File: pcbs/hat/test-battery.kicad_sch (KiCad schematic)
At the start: 15 parts, among them J2 Conn_01x02_Female, Q1 Q_NMOS_DGS, Q2 Q_NMOS_DGS, U2 INA195, U3 TP5000-Breakout-Akaddy

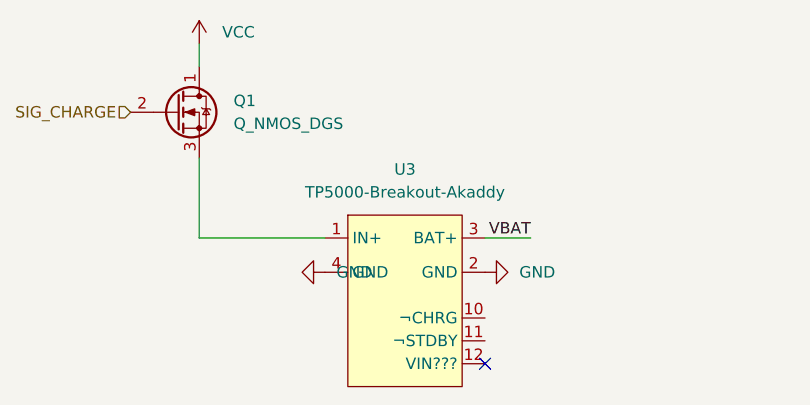
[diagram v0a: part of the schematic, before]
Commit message: fix symbol and footprint libraries
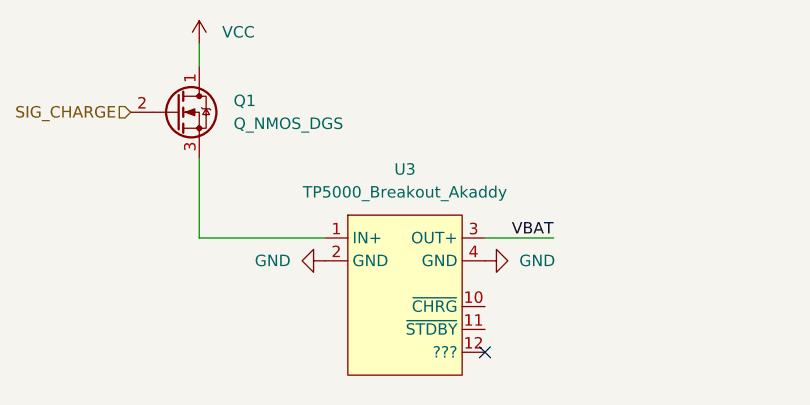
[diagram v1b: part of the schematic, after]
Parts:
- removed U3: TP5000-Breakout-Akaddy, symbol STS_Battery_Management:TP5000-Breakout-Akaddy
- added U3: TP5000_Breakout_Akaddy, symbol STS_Battery_Management:TP5000_Breakout_Akaddy
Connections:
- net GND: now also U3.2 (GND), U3.4 (GND)
- net VBAT: now also U3.3 (OUT+)
- net at Q1.3 (S): now also U3.1 (IN+)
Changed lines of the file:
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@@
   (junction (at 107.95 45.72) (diameter 0) (color 0 0 0 0)
   )
-  (no_connect (at 102.87 147.32))
+  (no_connect (at 102.87 146.05))
   (wire (pts (xy 71.12 133.35) (xy 85.09 133.35))
     (stroke (width 0) (type default) (color 0 0 0 0))
@@
     (stroke (width 0) (type default) (color 0 0 0 0))
   )
-  (wire (pts (xy 107.95 133.35) (xy 102.87 133.35))
+  (wire (pts (xy 102.87 133.35) (xy 110.49 133.35))
     (stroke (width 0) (type default) (color 0 0 0 0))
   )
@@
     (effects (font (size 1.27 1.27)) (justify left bottom))
   )
-  (label "VBAT" (at 107.95 133.35 180)
+  (label "VBAT" (at 110.49 133.35 180)
     (effects (font (size 1.27 1.27)) (justify right bottom))
   )
@@
     (pin "1")
   )
-  (symbol (lib_id "power:GND") (at 102.87 137.16 90) (unit 1)
-    (in_bom yes) (on_board yes) (fields_autoplaced)
-    (property "Reference" "#PWR0105" (id 0) (at 109.22 137.16 0)
-      (effects (font (size 1.27 1.27)) hide)
-    )
-    (property "Value" "GND" (id 1) (at 106.68 137.1599 90)
-      (effects (font (size 1.27 1.27)) (justify right))
-    )
-    (property "Footprint" "" (id 2) (at 102.87 137.16 0)
-      (effects (font (size 1.27 1.27)) hide)
-    )
-    (property "Datasheet" "" (id 3) (at 102.87 137.16 0)
+  (symbol (lib_id "STS_Battery_Management:TP5000_Breakout_Akaddy") (at 87.63 130.81 0) (unit 1)
+    (in_bom yes) (on_board yes) (fields_autoplaced)
+    (property "Reference" "U3" (id 0) (at 93.98 125.73 0))
+    (property "Value" "TP5000_Breakout_Akaddy" (id 1) (at 93.98 128.27 0))
+    (property "Footprint" "" (id 2) (at 87.63 129.54 0)
+      (effects (font (size 1.27 1.27)) hide)
+    )
+    (property "Datasheet" "https://www.amazon.de/Akaddy-TP5000-Lithium-Ionen-LiFePO4-Ladekarten-Lademodul/dp/B07X935CKF" (id 3) (at 87.63 129.54 0)
+      (effects (font (size 1.27 1.27)) hide)
+    )
+    (pin "1")
+    (pin "10")
+    (pin "11")
+    (pin "12")
+    (pin "2")
+    (pin "3")
+    (pin "4")
+  )
+  (symbol (lib_id "power:GND") (at 102.87 135.89 90) (unit 1)
+    (in_bom yes) (on_board yes)
+    (property "Reference" "#PWR0105" (id 0) (at 109.22 135.89 0)
+      (effects (font (size 1.27 1.27)) hide)
+    )
+    (property "Value" "GND" (id 1) (at 106.68 135.8899 90)
+      (effects (font (size 1.27 1.27)) (justify right))
+    )
+    (property "Footprint" "" (id 2) (at 102.87 135.89 0)
+      (effects (font (size 1.27 1.27)) hide)
+    )
+    (property "Datasheet" "" (id 3) (at 102.87 135.89 0)
       (effects (font (size 1.27 1.27)) hide)
     )
@@
     (pin "2")
   )
-  (symbol (lib_id "power:GND") (at 85.09 137.16 270) (unit 1)
-    (in_bom yes) (on_board yes) (fields_autoplaced)
-    (property "Reference" "#PWR0106" (id 0) (at 78.74 137.16 0)
-      (effects (font (size 1.27 1.27)) hide)
-    )
-    (property "Value" "GND" (id 1) (at 86.36 137.1599 90)
-      (effects (font (size 1.27 1.27)) (justify left))
-    )
-    (property "Footprint" "" (id 2) (at 85.09 137.16 0)
-      (effects (font (size 1.27 1.27)) hide)
-    )
-    (property "Datasheet" "" (id 3) (at 85.09 137.16 0)
+  (symbol (lib_id "power:GND") (at 85.09 135.89 270) (unit 1)
+    (in_bom yes) (on_board yes) (fields_autoplaced)
+    (property "Reference" "#PWR0106" (id 0) (at 78.74 135.89 0)
+      (effects (font (size 1.27 1.27)) hide)
+    )
+    (property "Value" "GND" (id 1) (at 81.28 135.8899 90)
+      (effects (font (size 1.27 1.27)) (justify right))
+    )
+    (property "Footprint" "" (id 2) (at 85.09 135.89 0)
+      (effects (font (size 1.27 1.27)) hide)
+    )
+    (property "Datasheet" "" (id 3) (at 85.09 135.89 0)
       (effects (font (size 1.27 1.27)) hide)
     )
@@
     (pin "2")
   )
-  (symbol (lib_id "STS_Battery_Management:TP5000-Breakout-Akaddy") (at 93.98 130.81 0) (unit 1)
-    (in_bom yes) (on_board yes) (fields_autoplaced)
-    (property "Reference" "U3" (id 0) (at 93.98 125.73 0))
-    (property "Value" "TP5000-Breakout-Akaddy" (id 1) (at 93.98 128.27 0))
-    (property "Footprint" "" (id 2) (at 90.17 133.35 0)
-      (effects (font (size 1.27 1.27)) hide)
-    )
-    (property "Datasheet" "" (id 3) (at 90.17 133.35 0)
-      (effects (font (size 1.27 1.27)) hide)
-    )
-    (pin "1")
-    (pin "10")
-    (pin "11")
-    (pin "12")
-    (pin "2")
-    (pin "3")
-    (pin "4")
-  )
   (symbol (lib_id "Device:R") (at 189.23 137.16 0) (unit 1)

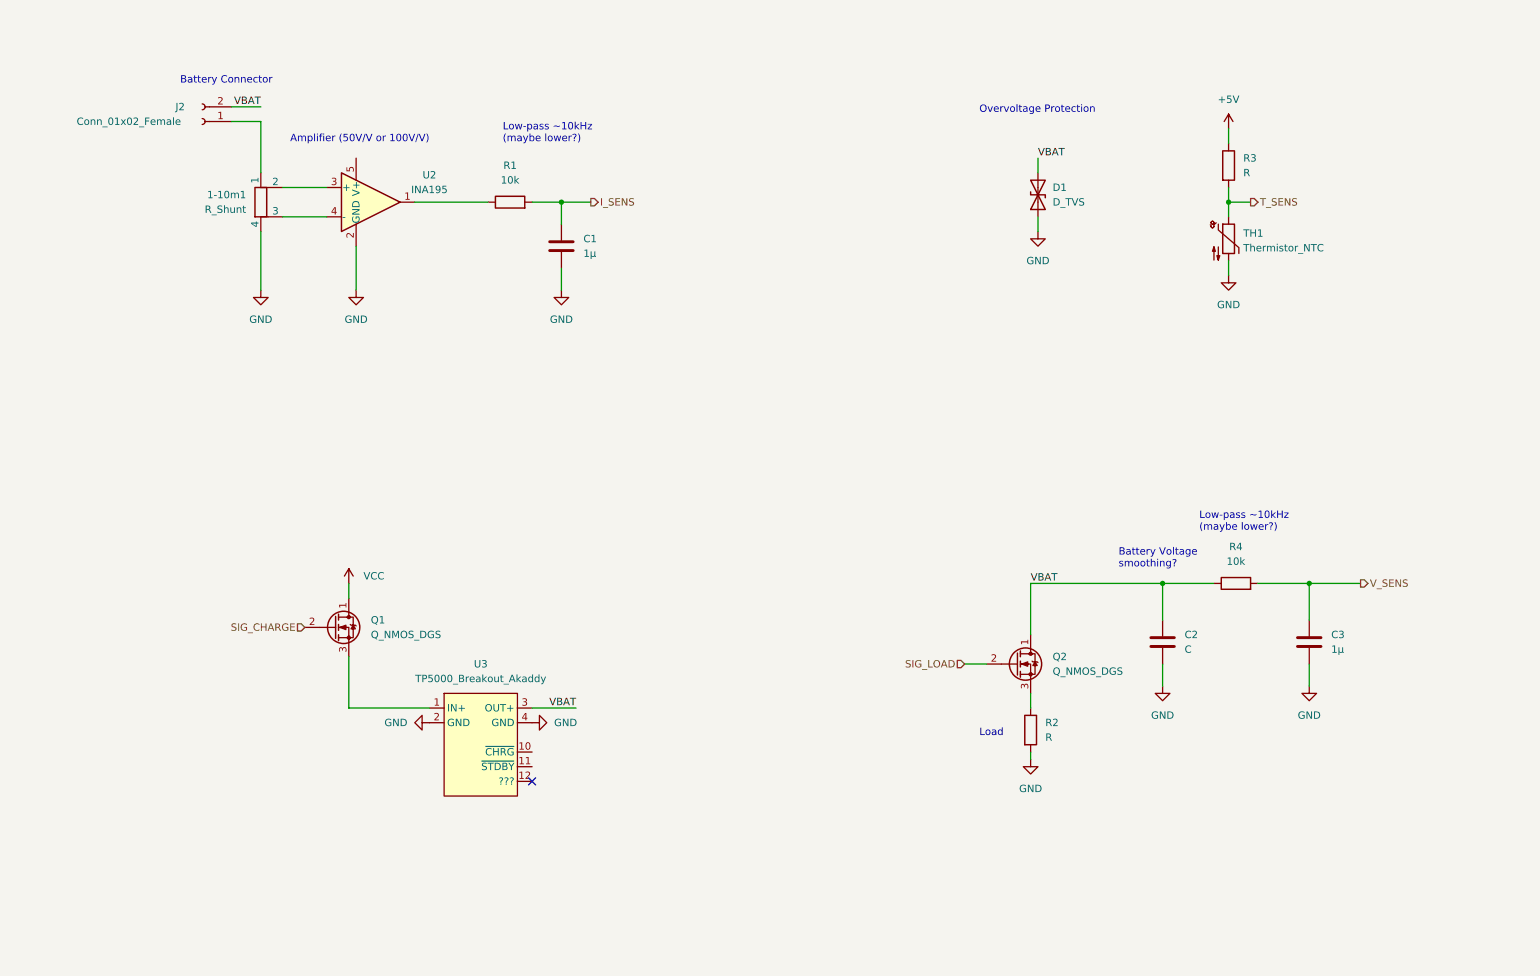
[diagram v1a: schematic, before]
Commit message: add ADCs
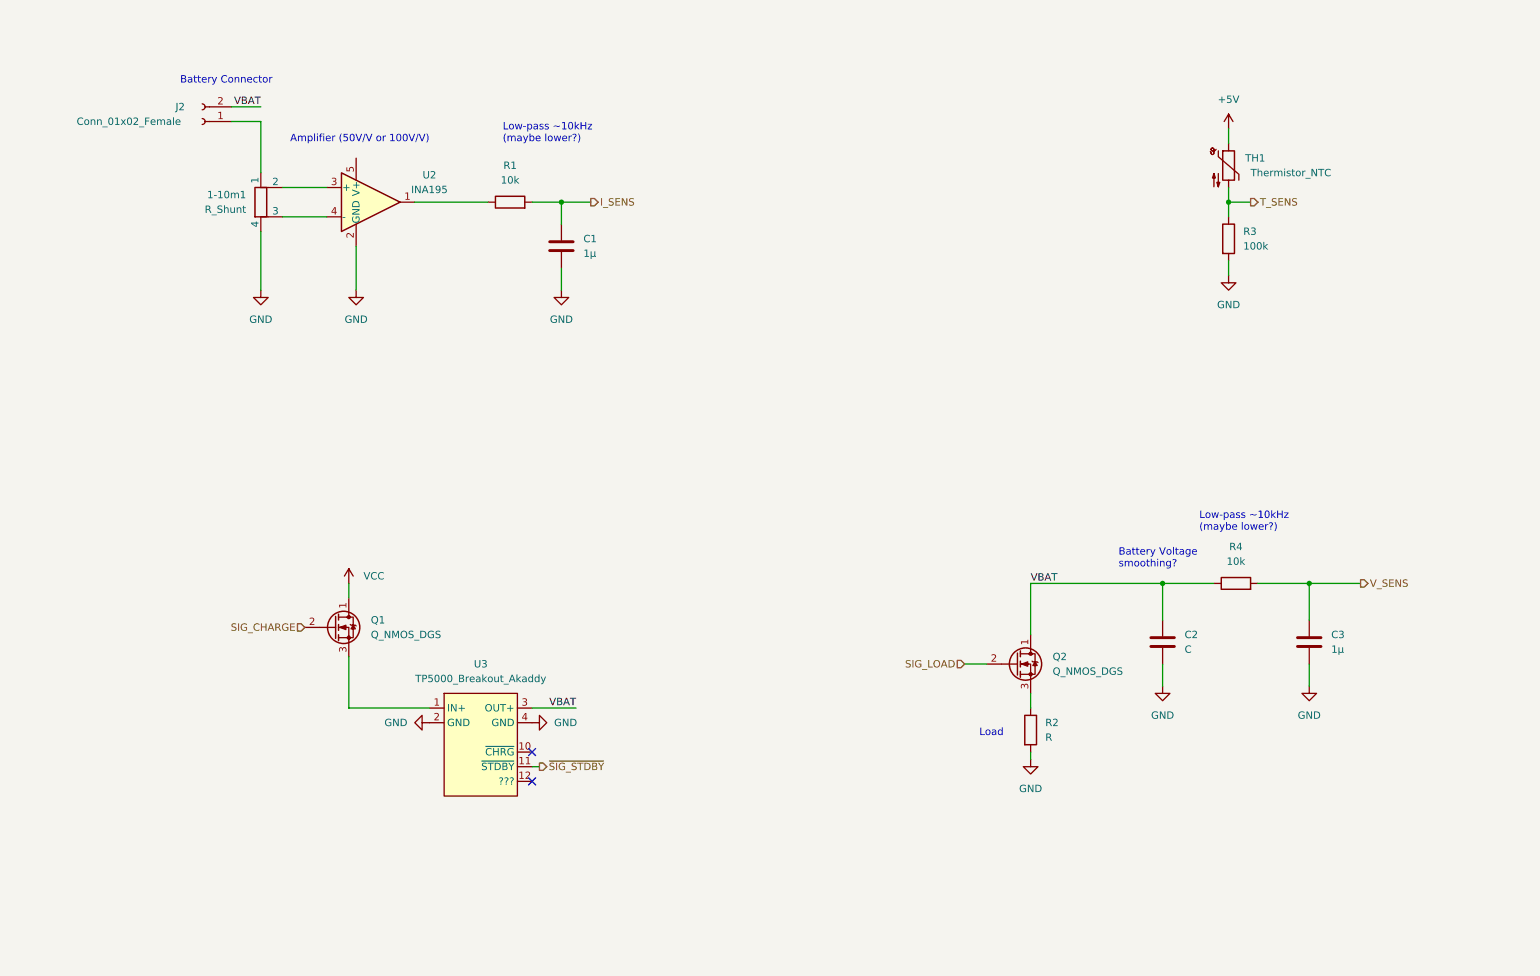
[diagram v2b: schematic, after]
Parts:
- removed D1: D_TVS, symbol Device:D_TVS
- C2: footprint Capacitor_SMD:C_0603_1608Metric -> (none)
- C3: footprint Capacitor_SMD:C_1206_3216Metric -> (none)
- J2: footprint (none) -> TerminalBlock:TerminalBlock_bornier-2_P5.08mm
- Q1, Q2: footprint Package_TO_SOT_THT:TO-251-3-1EP_Horizontal_TabDown -> (none)
- R3: value R -> 100k
- R4: footprint Resistor_SMD:R_0402_1005Metric -> (none)
- TH1: footprint (none) -> Connector_PinHeader_2.54mm:PinHeader_1x02_P2.54mm_Vertical
- U2: footprint Package_TO_SOT_SMD:SOT-23-5 -> (none)
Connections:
- net +5V: now also TH1.1; no longer R3.1
- net GND: now also R3.2; no longer TH1.2
- net T_SENS: now also R3.1, TH1.2; no longer R3.2, TH1.1
- net ~{SIG_STDBY}: now reaches U3.11 (~{STDBY})
- no-connect marks 1 -> 2
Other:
- note removed: "Overvoltage Protection"
- moved on the sheet: R3, TH1

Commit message: select parts for current and temperature sensors
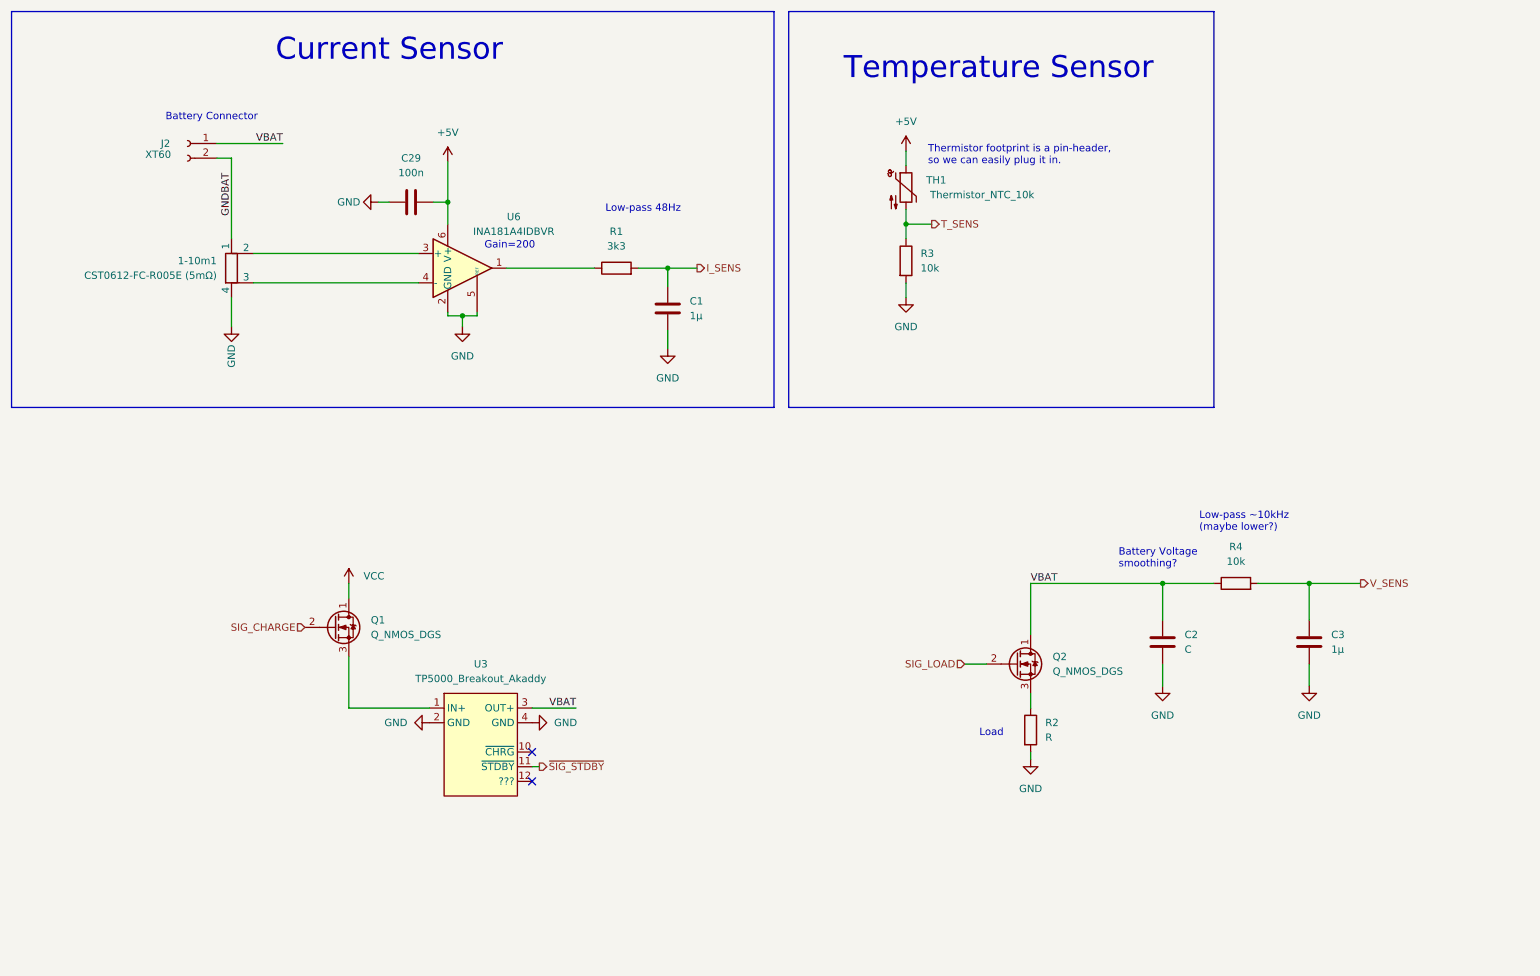
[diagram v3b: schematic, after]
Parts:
- removed U2: INA195, symbol Amplifier_Current:INA195
- added C29: 100n, Capacitor_SMD:C_0603_1608Metric, symbol Device:C
- added U6: INA181A4IDBVR, Package_TO_SOT_SMD:SOT-23-6, symbol Amplifier_Current:INA181
- 1-10m1: value R_Shunt -> CST0612-FC-R005E (5mΩ); footprint (none) -> STS_Resistor_SMD:CST0612-FC-R002E
- C1: footprint (none) -> Capacitor_SMD:C_0603_1608Metric
- J2: value Conn_01x02_Female -> XT60; footprint TerminalBlock:TerminalBlock_bornier-2_P5.08mm -> Connector_AMASS:AMASS_XT60-M_1x02_P7.20mm_Vertical
- R1: value 10k -> 3k3; footprint (none) -> Resistor_SMD:R_0603_1608Metric
- R3: value 100k -> 10k
- TH1: value Thermistor_NTC -> Thermistor_NTC_10k
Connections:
- net +5V: now also C29.2, U6.6 (V+)
- net GND: now also C29.1, U6.2 (GND), U6.5 (REF)
- net VBAT: now also J2.1 (Pin_1); no longer J2.2 (Pin_2)
- net at R1.1: now also U6.1
- net at 1-10m1.2: now also U6.3 (+)
- net at 1-10m1.3: now also U6.4 (-)
- net GNDBAT: now reaches 1-10m1.1
- net GNDBAT: now also J2.2 (Pin_2); no longer J2.1 (Pin_1)
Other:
- note added: "Current Sensor"
- note added: "Gain=200"
- note added: "Low-pass 48Hz"
- note added: "Temperature Sensor"
- note added: "Thermistor footprint is a pin-header, so we can easily plug it in."
- note removed: "Amplifier (50V/V or 100V/V)"
- moved on the sheet: 1-10m1, C1, J2, R1, R3, TH1

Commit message: work on charging circuit
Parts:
- added R35: 680, Resistor_SMD:R_0603_1608Metric, symbol Device:R
- added R36: 10k, Resistor_SMD:R_0603_1608Metric, symbol Device:R
- C3: footprint (none) -> Capacitor_SMD:C_0603_1608Metric
- R3: footprint (none) -> Resistor_SMD:R_0603_1608Metric
- R4: value 10k -> 3k3; footprint (none) -> Resistor_SMD:R_0603_1608Metric
- U3: footprint (none) -> STS_Boards:TP5000_Breakout_Akaddy
- renumbered C29 to C27, U6 to U2
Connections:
- net GND: now also Q1.3 (S), R36.2; no longer U3.2 (GND), U3.4 (GND)
- net SIG_CHARGE: now also R35.1; no longer Q1.2 (G)
- net VCC: now also U3.1 (IN+); no longer Q1.1 (D)
- net ~{SIG_STDBY} renamed ~{SIG_CHRG_DONE}
- new net: Q1.2 (G), R35.2, R36.1
- new net: Q1.1 (D), U3.2 (GND), U3.4 (GND)
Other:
- note added: "Breakout Pictures:"
- note added: "Charging"
- note added: "Datasheet TC5000 (Chip on Breakout)"
- note added: "V_{to} < 3V"
- note added: "max 8mA@3.3V"
- note removed: "Low-pass ~10kHz (maybe lower?)"
- moved on the sheet: Q2, R2, U3

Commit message: more work on charging circuit
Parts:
- removed C3: 1µ, Capacitor_SMD:C_0603_1608Metric, symbol Device:C
- removed Q2: Q_NMOS_DGS, symbol Device:Q_NMOS_DGS
- added #BT1: Battery, symbol Device:Battery_Cell
- added #R1: R_{intern}, symbol Device:R
- added C3: 220u, Capacitor_THT:CP_Radial_D6.3mm_P2.50mm, symbol Device:C_Polarized
- added C5: C, symbol Device:C
- added Q1: Q_NMOS_DGS, Package_TO_SOT_THT:TO-220-3_Vertical, symbol Device:Q_NMOS_DGS
- added R3: 680, Resistor_SMD:R_0603_1608Metric, symbol Device:R
- C2: value C -> 100n; footprint (none) -> Capacitor_SMD:C_0603_1608Metric
- Q2: renamed from Q1; footprint (none) -> Package_TO_SOT_SMD:SOT-223
- R2: value R -> 1; footprint (none) -> Resistor_THT:R_Axial_DIN0617_L17.0mm_D6.0mm_P25.40mm_Horizontal
- R4: value 3k3 -> 10k
- renumbered C27 to C1, C1 to C4, 1-10m1 to R1, R1 to R5, R3 to R6, R35 to R7, R36 to R8, U2 to U1, U3 to U2
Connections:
- net GND: now also R4.2, #BT1.2 (-), C3.2, C5.2, Q1.3 (S); no longer R2.2
- net SIG_LOAD: now also R3.1
- net V_SENS: now also J2.1 (Pin_1), R2.2, U2.3 (OUT+); no longer R4.2
- net at R2.1: now also C3.1, Q1.1 (D)
- net VBAT: no longer names the net of C2.1, R4.1
- net VBAT: now also Q1.2 (G), R3.2; no longer J2.1 (Pin_1), U2.3 (OUT+)
- new net: #BT1.1 (+), #R1.2
- no-connect marks 2 -> 3
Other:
- note added: "Battery"
- note added: "Battery looks like this"
- note added: "Can/Should we put a capacitor here to filter the signal a little?"
- note added: "Datasheet TP5000 (Chip on Breakout)"
- note added: "Discharging"
- note added: "Fake Load"
- note added: "Power Rating > 5W"
- note added: "V_{threshold} < 2V The signal is only 3.3V and the pull down creates a voltage divider"
- note removed: "Battery Voltage smoothing?"
- note removed: "Datasheet TC5000 (Chip on Breakout)"
- note removed: "Load"
- moved on the sheet: Q2, R7, R8, U2
